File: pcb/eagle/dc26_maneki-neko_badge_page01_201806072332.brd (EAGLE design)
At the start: 75.8 x 126.7 mm, 55 parts, among them T1 RK7002BMT116, U1 STM32F030C8T, U2 PAM2301CAAB330, U3 NPTC042KFMS-RC, U5 MIC2005A-1YM5-TR, U6 MIC2005A-1YM5-TR

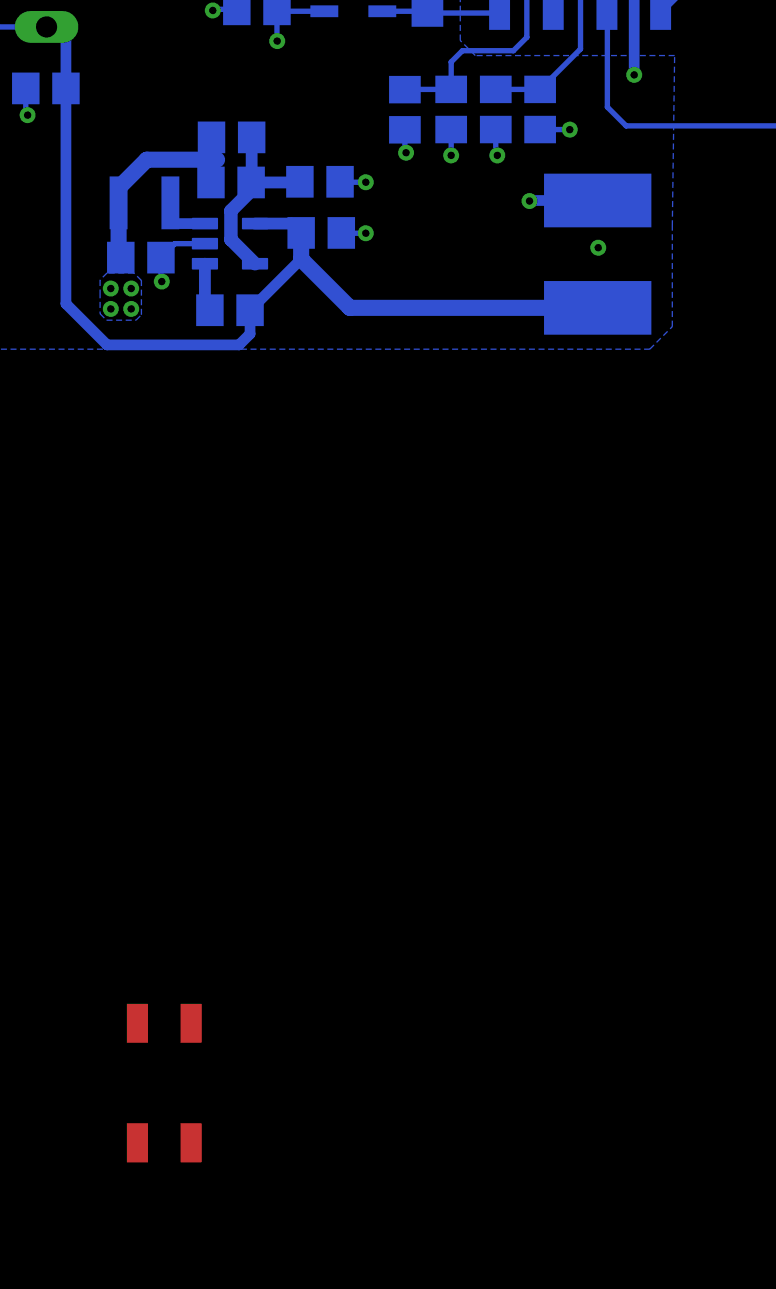
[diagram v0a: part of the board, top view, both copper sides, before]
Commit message: added copper art (nose, collar tag, and coin). just need to route shitty addon connector and i think its done
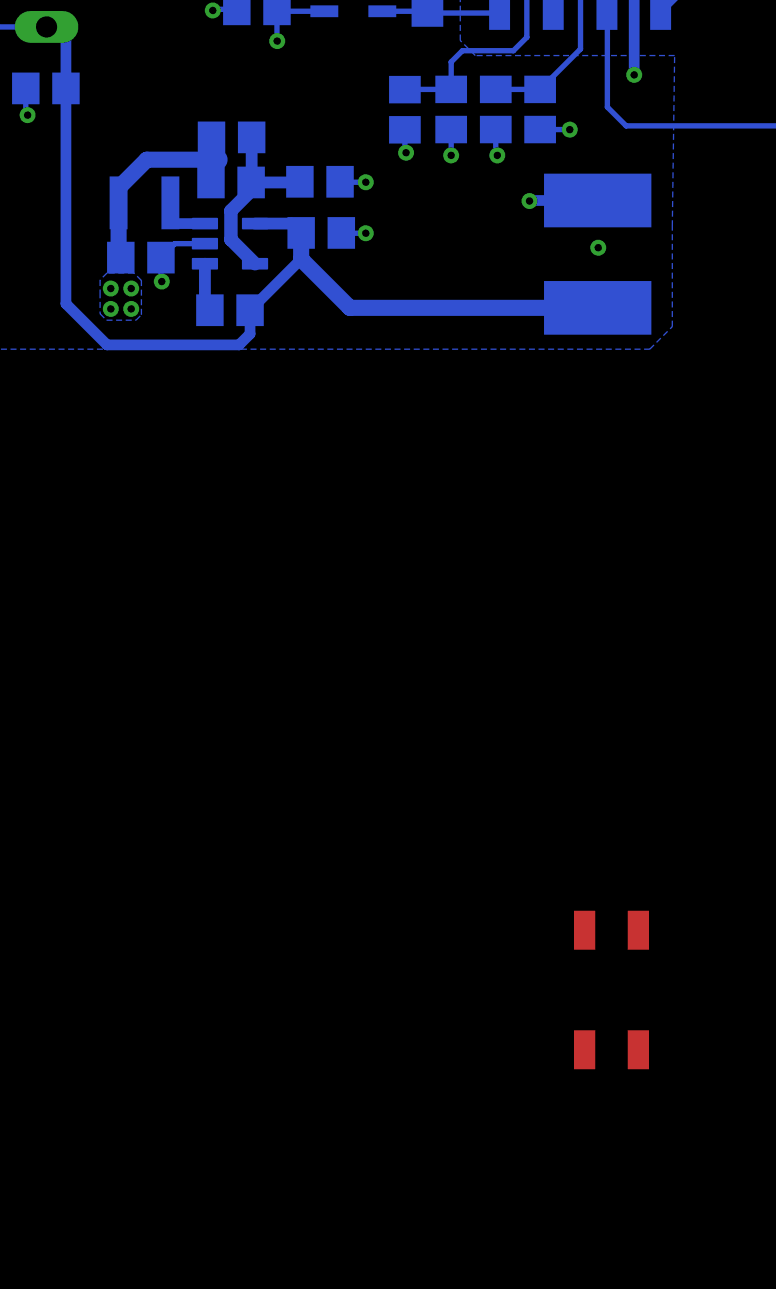
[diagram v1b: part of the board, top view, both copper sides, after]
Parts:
- moved H3 21.6 mm to (36.3, 17.5)
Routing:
- net 3V3: track 47.0 -> 49.4 mm
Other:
- board text added: "C:/Users/Daniel/Desktop/defcon26-meow/pcb/eagle/art prep/meow_v4_copper.bmp"

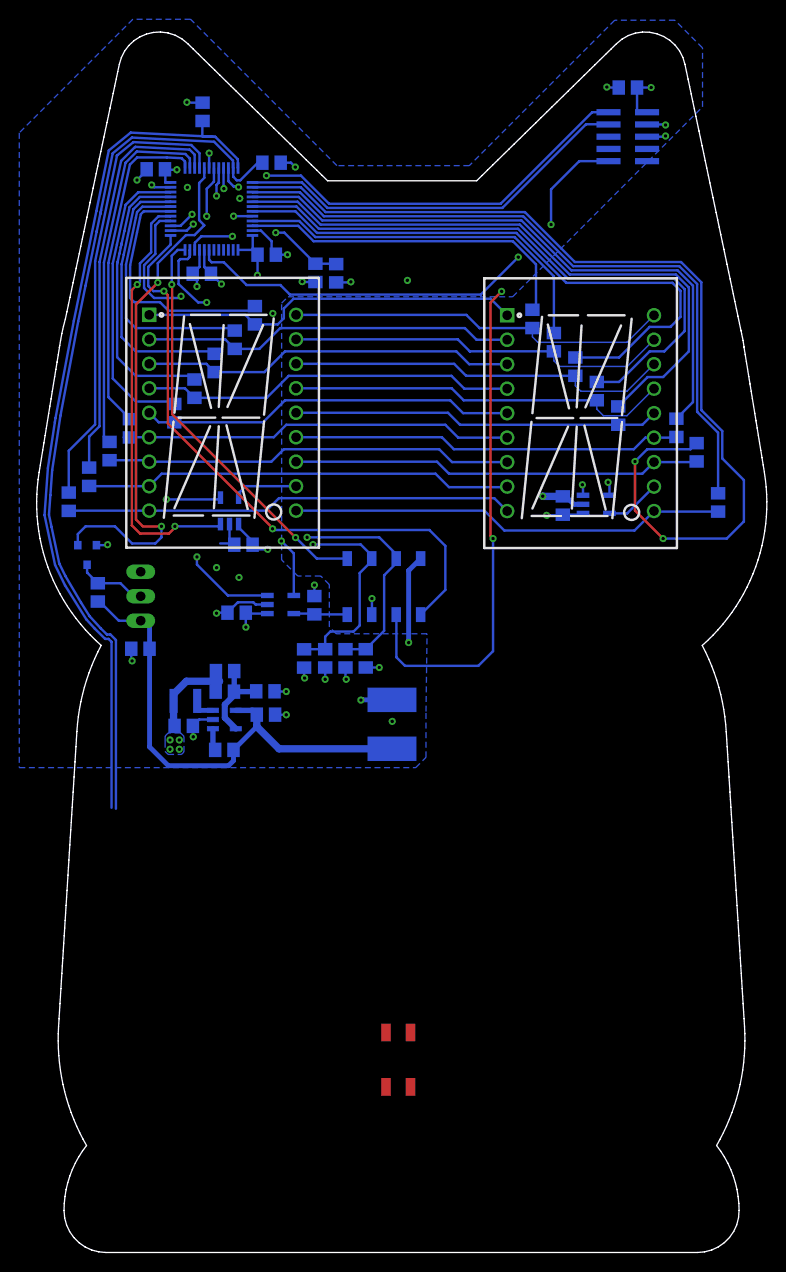
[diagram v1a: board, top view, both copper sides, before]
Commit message: silk fixed, drc errors fixed, going to export and send thru freedfm
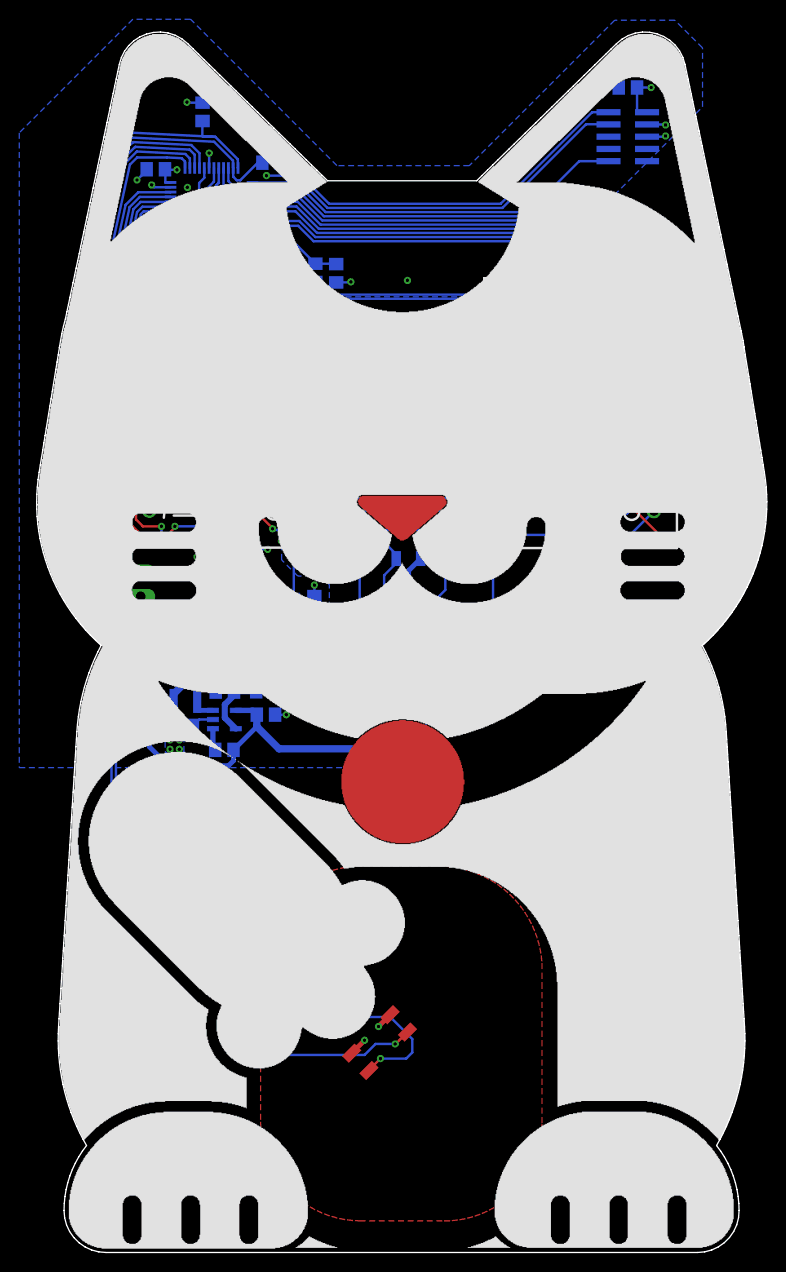
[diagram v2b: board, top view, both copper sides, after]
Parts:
- D1, D2: value (none) -> PSA08-11SRWA
- U4: value (none) -> MIC2005A-1YM5-TR
- moved H3 5.00 mm to (32.7, 21.0), turned to 315 degrees
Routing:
- net I2C1_SCL: track 90.4 -> 142.8 mm, vias 0 -> 1
- net I2C1_SDA: track 90.0 -> 137.5 mm, vias 0 -> 1
- net GND: track 92.9 -> 121.5 mm, vias 27 -> 28
- net 3V3: track 49.4 -> 78.0 mm, vias 16 -> 17
- added copper zone on layer 1, net N$4
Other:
- board text removed: "C:/Users/Daniel/Desktop/defcon26-meow/pcb/eagle/art prep/meow_v4_copper.bmp"
- board text removed: "C:/Users/Daniel/Desktop/defcon26-meow/pcb/eagle/art prep/meow_v4_whitesilk.bmp"
